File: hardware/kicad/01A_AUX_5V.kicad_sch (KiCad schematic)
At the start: 13 parts, among them U201 LM5164QDDARQ1 - AUX 5V CANDID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

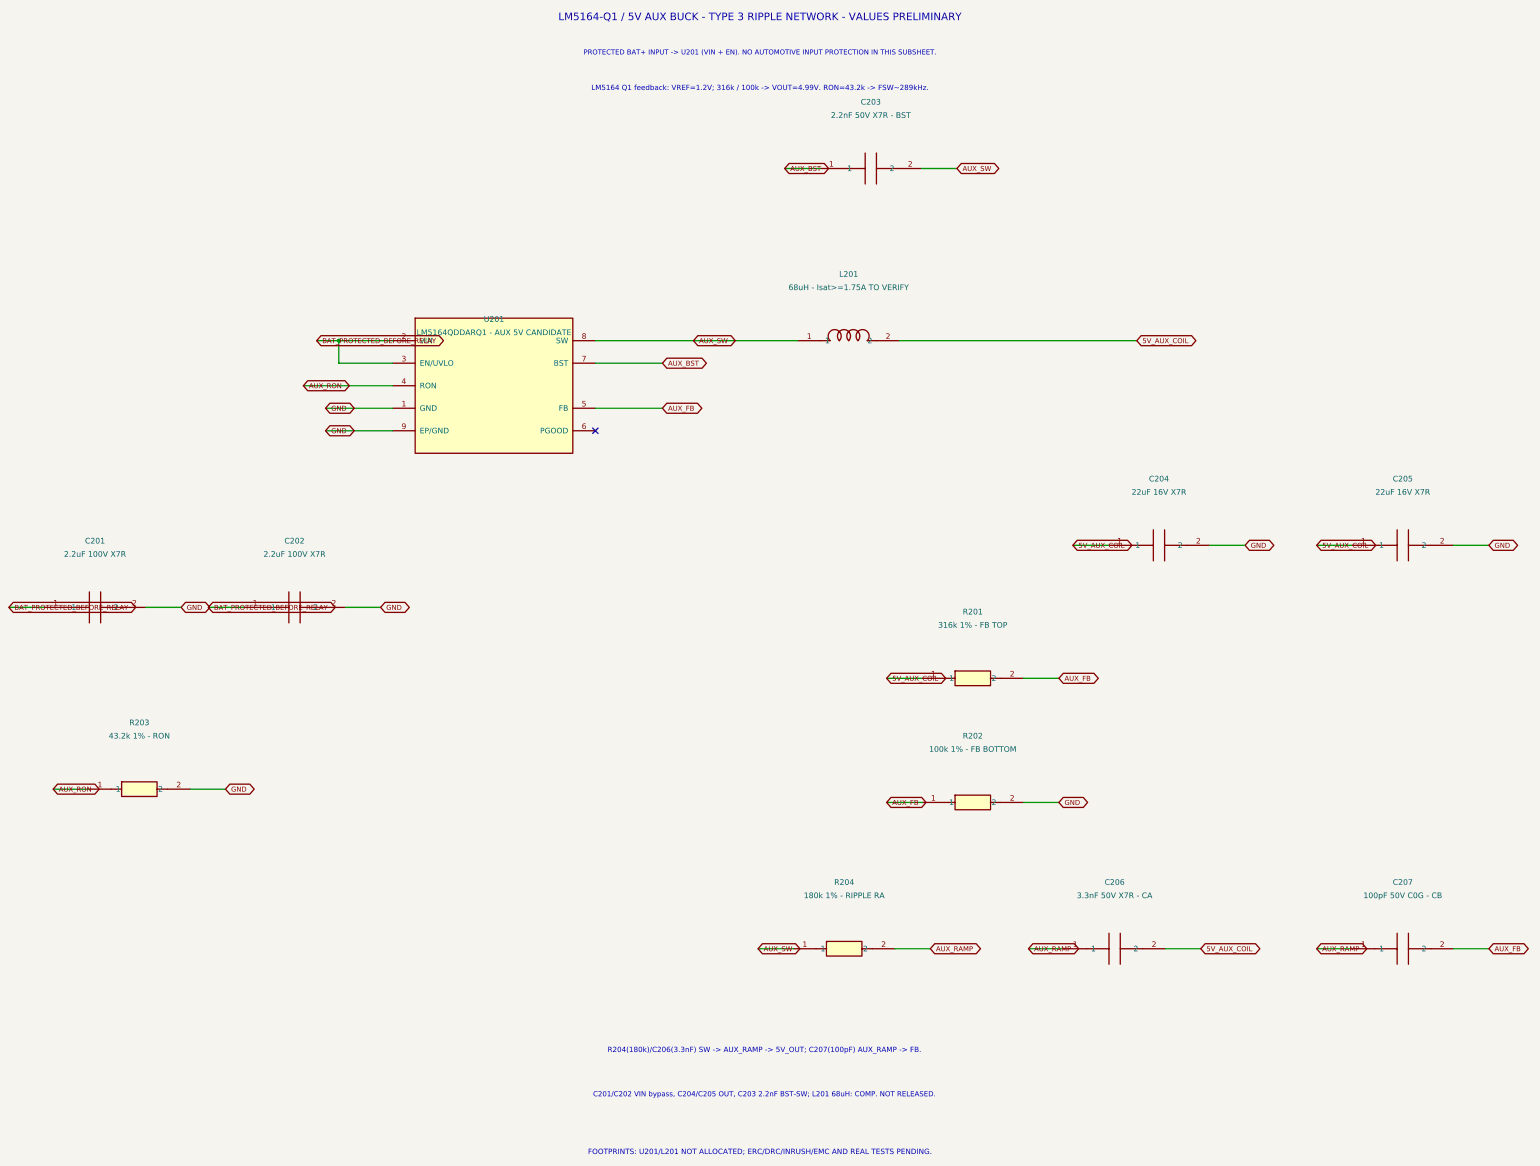
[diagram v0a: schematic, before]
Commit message: fix(kicad): eliminate eight reference collisions and gate hierarchy annotation
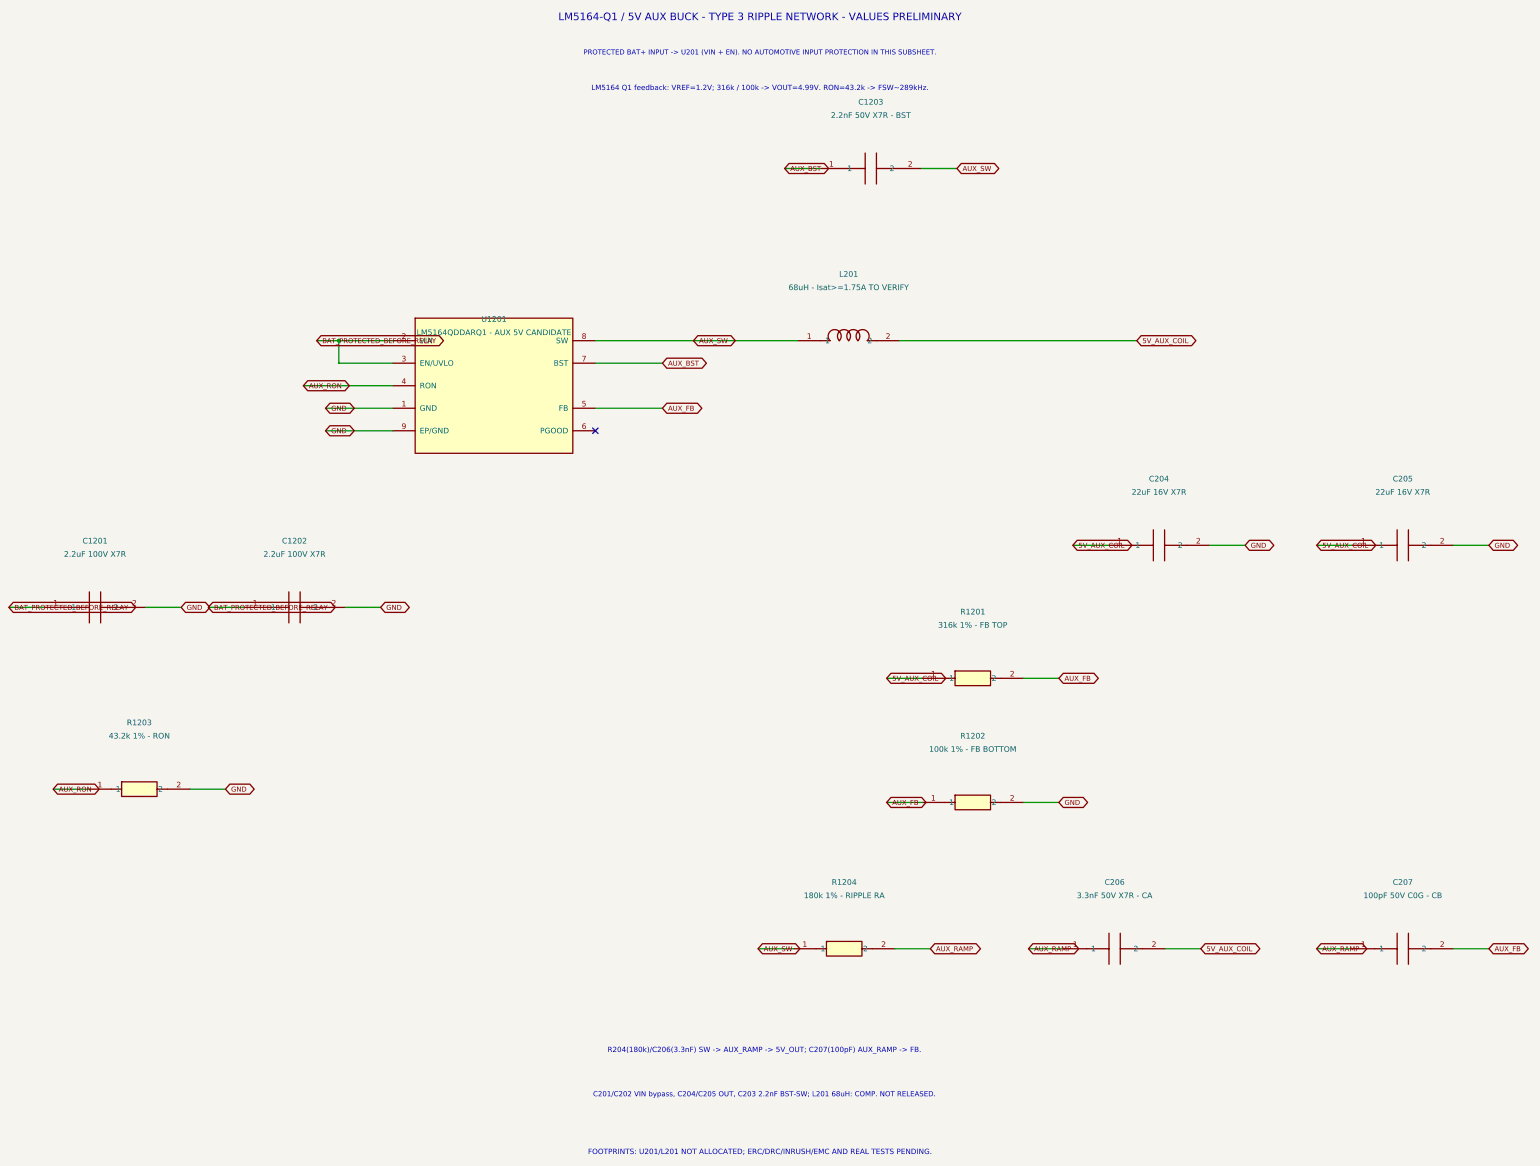
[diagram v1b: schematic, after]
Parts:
- renumbered C201 to C1201, C202 to C1202, C203 to C1203, R201 to R1201, R202 to R1202, R203 to R1203, R204 to R1204, U201 to U1201
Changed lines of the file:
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@@
  (title_block (title "TripTracer V1 - AUX 5V Relais-Spulenversorgung (Vorentwurf)") (date "2026-10-13") (rev "a1 / VALUES PRELIMINARY / ERC NOT RUN"))
  (symbol (lib_id "TripTracer_V1:LM5164_Q1") (at 145 105 0) (unit 1) (exclude_from_sim no) (in_bom yes) (on_board yes) (dnp no)
- (property "Reference" "U201" (at 145 90 0) (effects (font (size 1.27 1.27))))
+ (property "Reference" "U1201" (at 145 90 0) (effects (font (size 1.27 1.27))))
  (property "Value" "LM5164QDDARQ1 - AUX 5V CANDIDATE" (at 145 93 0) (effects (font (size 1.27 1.27))))
  (property "Footprint" "" (at 145 105 0) (effects (font (size 1.27 1.27)) (hide yes)))
  (pin "1") (pin "2") (pin "3") (pin "4") (pin "5") (pin "6") (pin "7") (pin "8") (pin "9")
- (instances (project "TripTracer_V1" (path "/a26d9b0c-7f10-4e5a-a65f-000000000064/a26d9b0c-7f10-4e5a-a65f-000000000065/d4c3b2a1-1111-4111-8111-222222222201" (reference "U201") (unit 1)))))
+ (instances (project "TripTracer_V1" (path "/a26d9b0c-7f10-4e5a-a65f-000000000064/a26d9b0c-7f10-4e5a-a65f-000000000065/d4c3b2a1-1111-4111-8111-222222222201" (reference "U1201") (unit 1)))))
 (symbol (lib_id "Tripmaster_Sym:L") (at 225 94.84 0) (unit 1) (exclude_from_sim no) (in_bom yes) (on_board yes) (dnp no)
  (property "Reference" "L201" (at 225 79.84 0) (effects (font (size 1.27 1.27))))
@@
  (instances (project "TripTracer_V1" (path "/a26d9b0c-7f10-4e5a-a65f-000000000064/a26d9b0c-7f10-4e5a-a65f-000000000065/d4c3b2a1-1111-4111-8111-222222222201" (reference "L201") (unit 1)))))
 (symbol (lib_id "Tripmaster_Sym:C1210") (at 55 155 0) (unit 1) (exclude_from_sim no) (in_bom yes) (on_board yes) (dnp no)
- (property "Reference" "C201" (at 55 140 0) (effects (font (size 1.27 1.27))))
+ (property "Reference" "C1201" (at 55 140 0) (effects (font (size 1.27 1.27))))
  (property "Value" "2.2uF 100V X7R" (at 55 143 0) (effects (font (size 1.27 1.27))))
  (property "Footprint" "Tripmaster:C_1210_3225" (at 55 155 0) (effects (font (size 1.27 1.27)) (hide yes)))
  (pin "1") (pin "2")
- (instances (project "TripTracer_V1" (path "/a26d9b0c-7f10-4e5a-a65f-000000000064/a26d9b0c-7f10-4e5a-a65f-000000000065/d4c3b2a1-1111-4111-8111-222222222201" (reference "C201") (unit 1)))))
+ (instances (project "TripTracer_V1" (path "/a26d9b0c-7f10-4e5a-a65f-000000000064/a26d9b0c-7f10-4e5a-a65f-000000000065/d4c3b2a1-1111-4111-8111-222222222201" (reference "C1201") (unit 1)))))
 (symbol (lib_id "Tripmaster_Sym:C1210") (at 100 155 0) (unit 1) (exclude_from_sim no) (in_bom yes) (on_board yes) (dnp no)
- (property "Reference" "C202" (at 100 140 0) (effects (font (size 1.27 1.27))))
+ (property "Reference" "C1202" (at 100 140 0) (effects (font (size 1.27 1.27))))
  (property "Value" "2.2uF 100V X7R" (at 100 143 0) (effects (font (size 1.27 1.27))))
  (property "Footprint" "Tripmaster:C_1210_3225" (at 100 155 0) (effects (font (size 1.27 1.27)) (hide yes)))
  (pin "1") (pin "2")
- (instances (project "TripTracer_V1" (path "/a26d9b0c-7f10-4e5a-a65f-000000000064/a26d9b0c-7f10-4e5a-a65f-000000000065/d4c3b2a1-1111-4111-8111-222222222201" (reference "C202") (unit 1)))))
+ (instances (project "TripTracer_V1" (path "/a26d9b0c-7f10-4e5a-a65f-000000000064/a26d9b0c-7f10-4e5a-a65f-000000000065/d4c3b2a1-1111-4111-8111-222222222201" (reference "C1202") (unit 1)))))
 (symbol (lib_id "Tripmaster_Sym:C") (at 230 56 0) (unit 1) (exclude_from_sim no) (in_bom yes) (on_board yes) (dnp no)
- (property "Reference" "C203" (at 230 41 0) (effects (font (size 1.27 1.27))))
+ (property "Reference" "C1203" (at 230 41 0) (effects (font (size 1.27 1.27))))
  (property "Value" "2.2nF 50V X7R - BST" (at 230 44 0) (effects (font (size 1.27 1.27))))
  (property "Footprint" "Tripmaster:C_1206_3216" (at 230 56 0) (effects (font (size 1.27 1.27)) (hide yes)))
  (pin "1") (pin "2")
- (instances (project "TripTracer_V1" (path "/a26d9b0c-7f10-4e5a-a65f-000000000064/a26d9b0c-7f10-4e5a-a65f-000000000065/d4c3b2a1-1111-4111-8111-222222222201" (reference "C203") (unit 1)))))
+ (instances (project "TripTracer_V1" (path "/a26d9b0c-7f10-4e5a-a65f-000000000064/a26d9b0c-7f10-4e5a-a65f-000000000065/d4c3b2a1-1111-4111-8111-222222222201" (reference "C1203") (unit 1)))))
 (symbol (lib_id "Tripmaster_Sym:C1210") (at 295 141 0) (unit 1) (exclude_from_sim no) (in_bom yes) (on_board yes) (dnp no)
  (property "Reference" "C204" (at 295 126 0) (effects (font (size 1.27 1.27))))
@@
  (instances (project "TripTracer_V1" (path "/a26d9b0c-7f10-4e5a-a65f-000000000064/a26d9b0c-7f10-4e5a-a65f-000000000065/d4c3b2a1-1111-4111-8111-222222222201" (reference "C207") (unit 1)))))
 (symbol (lib_id "Tripmaster_Sym:R") (at 253 171 0) (unit 1) (exclude_from_sim no) (in_bom yes) (on_board yes) (dnp no)
- (property "Reference" "R201" (at 253 156 0) (effects (font (size 1.27 1.27))))
+ (property "Reference" "R1201" (at 253 156 0) (effects (font (size 1.27 1.27))))
  (property "Value" "316k 1% - FB TOP" (at 253 159 0) (effects (font (size 1.27 1.27))))
  (property "Footprint" "Tripmaster:R_1206_3216" (at 253 171 0) (effects (font (size 1.27 1.27)) (hide yes)))
  (pin "1") (pin "2")
- (instances (project "TripTracer_V1" (path "/a26d9b0c-7f10-4e5a-a65f-000000000064/a26d9b0c-7f10-4e5a-a65f-000000000065/d4c3b2a1-1111-4111-8111-222222222201" (reference "R201") (unit 1)))))
+ (instances (project "TripTracer_V1" (path "/a26d9b0c-7f10-4e5a-a65f-000000000064/a26d9b0c-7f10-4e5a-a65f-000000000065/d4c3b2a1-1111-4111-8111-222222222201" (reference "R1201") (unit 1)))))
 (symbol (lib_id "Tripmaster_Sym:R") (at 253 199 0) (unit 1) (exclude_from_sim no) (in_bom yes) (on_board yes) (dnp no)
- (property "Reference" "R202" (at 253 184 0) (effects (font (size 1.27 1.27))))
+ (property "Reference" "R1202" (at 253 184 0) (effects (font (size 1.27 1.27))))
  (property "Value" "100k 1% - FB BOTTOM" (at 253 187 0) (effects (font (size 1.27 1.27))))
  (property "Footprint" "Tripmaster:R_1206_3216" (at 253 199 0) (effects (font (size 1.27 1.27)) (hide yes)))
  (pin "1") (pin "2")
- (instances (project "TripTracer_V1" (path "/a26d9b0c-7f10-4e5a-a65f-000000000064/a26d9b0c-7f10-4e5a-a65f-000000000065/d4c3b2a1-1111-4111-8111-222222222201" (reference "R202") (unit 1)))))
+ (instances (project "TripTracer_V1" (path "/a26d9b0c-7f10-4e5a-a65f-000000000064/a26d9b0c-7f10-4e5a-a65f-000000000065/d4c3b2a1-1111-4111-8111-222222222201" (reference "R1202") (unit 1)))))
 (symbol (lib_id "Tripmaster_Sym:R") (at 65 196 0) (unit 1) (exclude_from_sim no) (in_bom yes) (on_board yes) (dnp no)
- (property "Reference" "R203" (at 65 181 0) (effects (font (size 1.27 1.27))))
+ (property "Reference" "R1203" (at 65 181 0) (effects (font (size 1.27 1.27))))
  (property "Value" "43.2k 1% - RON" (at 65 184 0) (effects (font (size 1.27 1.27))))
  (property "Footprint" "Tripmaster:R_1206_3216" (at 65 196 0) (effects (font (size 1.27 1.27)) (hide yes)))
  (pin "1") (pin "2")
- (instances (project "TripTracer_V1" (path "/a26d9b0c-7f10-4e5a-a65f-000000000064/a26d9b0c-7f10-4e5a-a65f-000000000065/d4c3b2a1-1111-4111-8111-222222222201" (reference "R203") (unit 1)))))
+ (instances (project "TripTracer_V1" (path "/a26d9b0c-7f10-4e5a-a65f-000000000064/a26d9b0c-7f10-4e5a-a65f-000000000065/d4c3b2a1-1111-4111-8111-222222222201" (reference "R1203") (unit 1)))))
 (symbol (lib_id "Tripmaster_Sym:R") (at 224 232 0) (unit 1) (exclude_from_sim no) (in_bom yes) (on_board yes) (dnp no)
- (property "Reference" "R204" (at 224 217 0) (effects (font (size 1.27 1.27))))
+ (property "Reference" "R1204" (at 224 217 0) (effects (font (size 1.27 1.27))))
  (property "Value" "180k 1% - RIPPLE RA" (at 224 220 0) (effects (font (size 1.27 1.27))))
  (property "Footprint" "Tripmaster:R_1206_3216" (at 224 232 0) (effects (font (size 1.27 1.27)) (hide yes)))
  (pin "1") (pin "2")
- (instances (project "TripTracer_V1" (path "/a26d9b0c-7f10-4e5a-a65f-000000000064/a26d9b0c-7f10-4e5a-a65f-000000000065/d4c3b2a1-1111-4111-8111-222222222201" (reference "R204") (unit 1)))))
+ (instances (project "TripTracer_V1" (path "/a26d9b0c-7f10-4e5a-a65f-000000000064/a26d9b0c-7f10-4e5a-a65f-000000000065/d4c3b2a1-1111-4111-8111-222222222201" (reference "R1204") (unit 1)))))
 (wire (pts (xy 167.86 94.84) (xy 213.57 94.84)) (stroke (width 0) (type default)))
 (global_label "AUX_SW" (shape bidirectional) (at 190 94.84 0) (effects (font (size 1.12 1.12)) (justify left)))
